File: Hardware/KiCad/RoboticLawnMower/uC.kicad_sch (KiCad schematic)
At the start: 11 parts, among them J12 Conn_02x05_Row_Letter_Last, U2 AVR128DB48x-xPT, Y1 32.768kHz

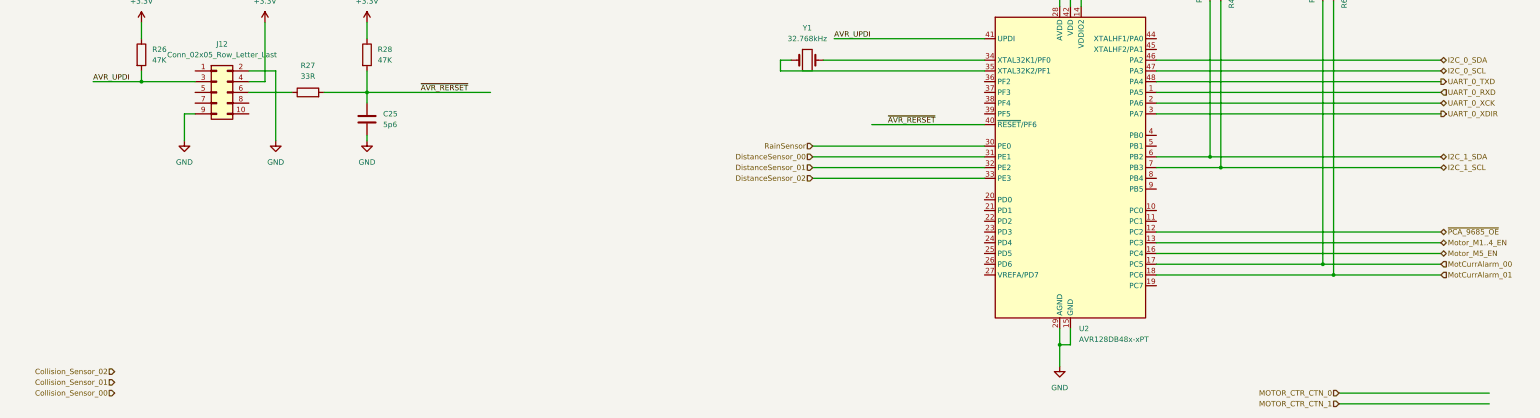
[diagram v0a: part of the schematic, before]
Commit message: Schaltplan & Layout Änderung
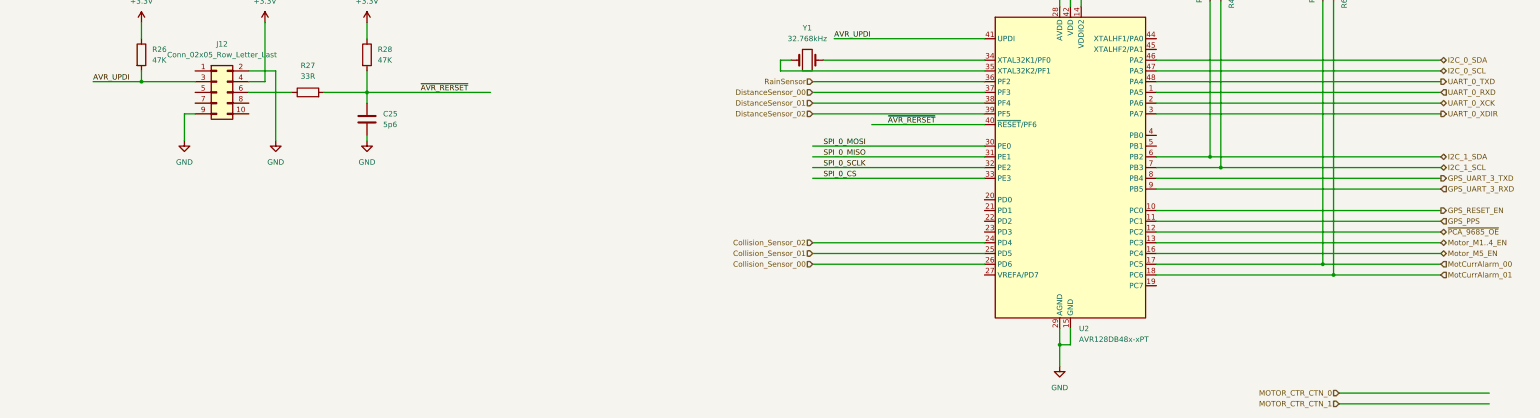
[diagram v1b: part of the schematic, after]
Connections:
- net Collision_Sensor_00: now also U2.26 (PD6)
- net Collision_Sensor_01: now also U2.25 (PD5)
- net Collision_Sensor_02: now also U2.24 (PD4)
- net DistanceSensor_00: now also U2.37 (PF3); no longer U2.31 (PE1)
- net DistanceSensor_01: now also U2.38 (PF4); no longer U2.32 (PE2)
- net DistanceSensor_02: now also U2.39 (PF5); no longer U2.33 (PE3)
- net RainSensor: now also U2.36 (PF2); no longer U2.30 (PE0)
- net GPS_RESET_EN: now reaches U2.10 (PC0)
- net GPS_PPS: now reaches U2.11 (PC1)
- net GPS_UART_3_TXD: now reaches U2.8 (PB4)
- net GPS_UART_3_RXD: now reaches U2.9 (PB5)
- new net SPI_0_CS: U2.33 (PE3)
- new net SPI_0_MISO: U2.31 (PE1)
- new net SPI_0_MOSI: U2.30 (PE0)
- new net SPI_0_SCLK: U2.32 (PE2)

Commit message: Layout ready add gerber file
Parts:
- added C11, C13, C23, C24: 100n, Capacitor_SMD:C_0603_1608Metric, symbol Device:C
- added C34: 1u, Capacitor_SMD:C_0603_1608Metric, symbol Device:C
- added R19, R20, R21: 4k7, Resistor_SMD:R_0603_1608Metric, symbol Device:R
- added U5: W25Q128JVS, Package_SO:SOIC-8_5.23x5.23mm_P1.27mm, symbol Memory_Flash:W25Q128JVS
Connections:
- net +3.3V: now also C11.1, C13.1, C23.1, C24.1, C34.1, R19.2, R20.2, R21.2, U5.8 (VCC)
- net GND: now also C11.2, C13.2, C23.2, C24.2, C34.2, U5.4 (GND)
- net MOTOR_CTR_CTN_0: now also U2.44 (XTALHF1/PA0)
- net MOTOR_CTR_CTN_1: now also U2.20 (PD0)
- net Motor_M5_EN: now also U2.12 (PC2); no longer U2.16 (PC4)
- net SPI_0_CS: now also R19.1, U5.1 (~{CS})
- net SPI_0_MISO: now also U5.2 (DO(IO1))
- net SPI_0_MOSI: now also U5.5 (DI(IO0))
- net SPI_0_SCLK: now also U5.6 (CLK)
- net ~{PCA_9685_OE}: now also U2.16 (PC4); no longer U2.12 (PC2)
- net WLAN_MOD_EN: now reaches U2.4 (PB0)
- net GPS_MOD_EN: now reaches U2.5 (PB1)
- new net: R21.1, U5.7 (IO3)
- new net: R20.1, U5.3 (IO2)
